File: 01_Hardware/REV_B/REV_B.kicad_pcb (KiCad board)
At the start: 2 copper layers, 65 x 30 mm, 79 parts, among them J1 RaspberryPi, J10 Conn_01x03, J11 Conn_01x03, J12 Conn_01x03, J13 Conn_01x08, J2 Conn_01x02, J3 Conn_01x02, J4 Conn_01x02, J5 Conn_01x08, J6 Conn_02x04_Counter_Clockwise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

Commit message: Routing in progress
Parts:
- C1: moved to B.Cu
- moved R18 17.4 mm to (40.1, 17.7)
- moved R19 15.5 mm to (40.1, 19.3)
- moved R20 14.3 mm to (40.1, 20.8)
- moved R29 11.4 mm to (34.5, 17.4), turned to 0 degrees
- moved C3 10.5 mm to (51.6, 18.3)
- moved R46 7.09 mm to (34.5, 20.8)
- moved R47 7.09 mm to (34.5, 19.1)
- moved R9 5.98 mm to (32.3, 9.53), turned to 270 degrees
- moved U3 4.24 mm to (37.7, 11.3)
- moved J6 2.95 mm to (34.8, 13.5), turned to 270 degrees
- moved J9 2.16 mm to (31.2, 22.9)
- moved J7 2.03 mm to (37.6, 22.9)
- moved J8 1.91 mm to (34.5, 22.9)
- moved R28 1.48 mm to (44.6, 19.2)
- moved R27 1.27 mm to (44.6, 17.7)
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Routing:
- net +3V3: track 71.9 -> 147.2 mm, vias 4 -> 6
- net +BATT: track 0.00 -> 30.0 mm, vias 0 -> 2
- net +5V: track 58.2 -> 85.0 mm
- net Net-(D1-Pad3): track 0.00 -> 25.3 mm, vias 0 -> 1
- net Net-(D1-Pad2): track 0.00 -> 23.4 mm, vias 0 -> 1
- net Net-(D1-Pad4): track 0.00 -> 21.8 mm, vias 0 -> 1
- net Net-(J1-Pad35): track 0.00 -> 16.0 mm
- net Net-(J3-Pad2): track 0.00 -> 15.7 mm
- net GND: track 0.00 -> 15.6 mm, vias 0 -> 6
- net Net-(J1-Pad40): track 0.00 -> 15.0 mm, vias 0 -> 1
- net Net-(C10-Pad1): track 3.94 -> 17.8 mm
- net Net-(J1-Pad37): track 0.00 -> 13.6 mm, vias 0 -> 1
- net Net-(J1-Pad36): track 0.00 -> 13.5 mm
- net Net-(J5-Pad8): track 0.00 -> 12.6 mm, vias 0 -> 1
- net Net-(J1-Pad32): track 0.00 -> 12.4 mm
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
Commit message: Routing almost done
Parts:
- moved C4 0.76 mm to (25.9, 8.26)
- moved R10 0.76 mm to (24.1, 8.26)
- moved R1 0.38 mm to (27.9, 8.26)
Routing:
- net SPI0_CS1_LV: track 0.00 -> 61.9 mm, vias 0 -> 3
- net GND: track 15.6 -> 75.2 mm, vias 6 -> 13
- net I2C1_SDA_HV: track 7.45 -> 56.6 mm
- net SPI0_MISO_LV: track 1.81 -> 50.2 mm, vias 0 -> 4
- net +5V: track 85.0 -> 129.1 mm, vias 4 -> 7
- net SPI0_CLK_LV: track 0.00 -> 40.3 mm, vias 0 -> 1
- net SPI0_MOSI_LV: track 1.88 -> 37.6 mm, vias 0 -> 2
- net I2C1_SCL_HV: track 12.2 -> 40.7 mm, vias 0 -> 2
- net Net-(J6-Pad8): track 0.00 -> 20.5 mm, vias 0 -> 1
- net Net-(J1-Pad24): track 0.00 -> 20.5 mm
- net Net-(J6-Pad2): track 0.00 -> 18.6 mm, vias 0 -> 1
- net Net-(J6-Pad4): track 0.00 -> 18.5 mm, vias 0 -> 1
- net Net-(J6-Pad6): track 0.00 -> 18.2 mm, vias 0 -> 1
- net Net-(R46-Pad2): track 9.14 -> 26.9 mm, vias 2 -> 0
- net Net-(J6-Pad7): track 0.00 -> 17.5 mm, vias 0 -> 1
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
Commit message: routing done
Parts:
- moved C3 0.85 mm to (51.9, 17.5)
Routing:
- net GND: track 75.2 -> 82.0 mm, vias 13 -> 17
- net Net-(J1-Pad37): track 13.7 -> 16.5 mm
- net +3V3: track 156.4 -> 159.0 mm
- net Net-(J1-Pad38): track 9.13 -> 11.3 mm
- net Net-(J6-Pad8): track 20.5 -> 18.6 mm
- net SPI0_MISO_LV: track 50.2 -> 48.4 mm

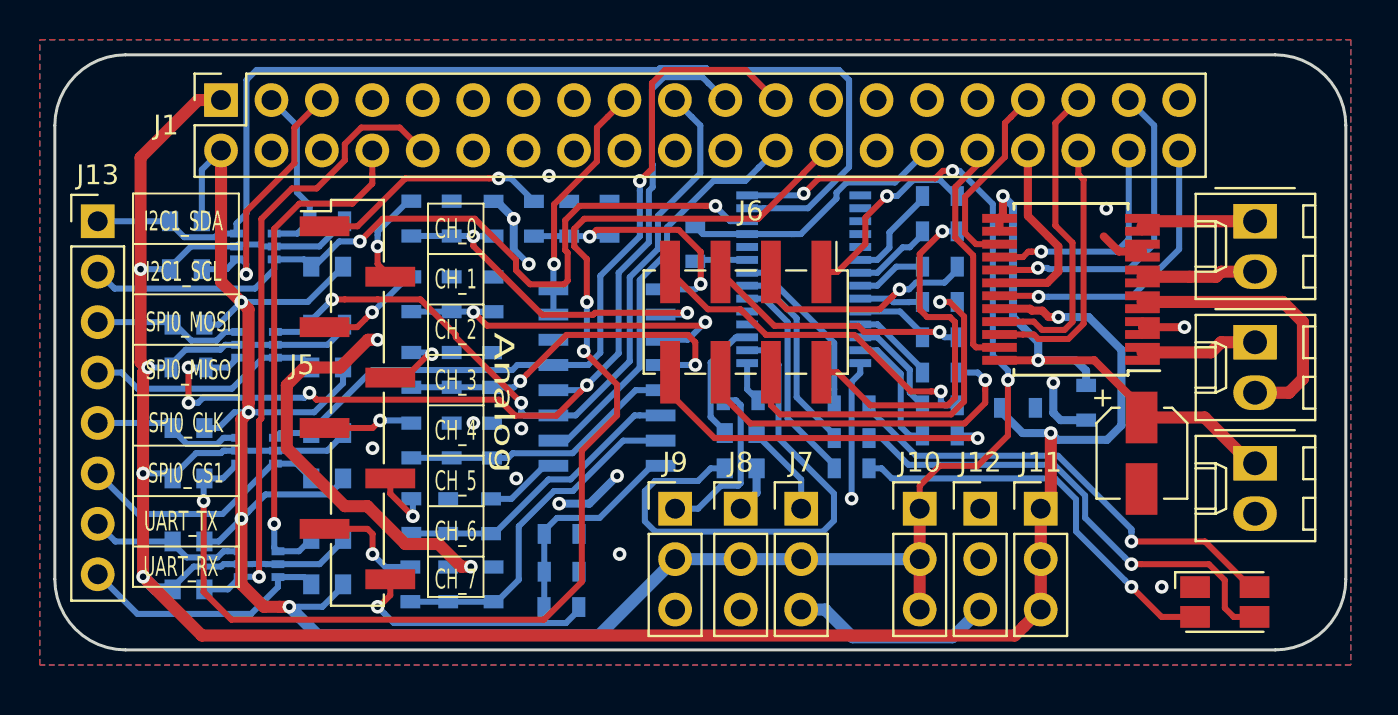
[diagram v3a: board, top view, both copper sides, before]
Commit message: Taster added. routing not done
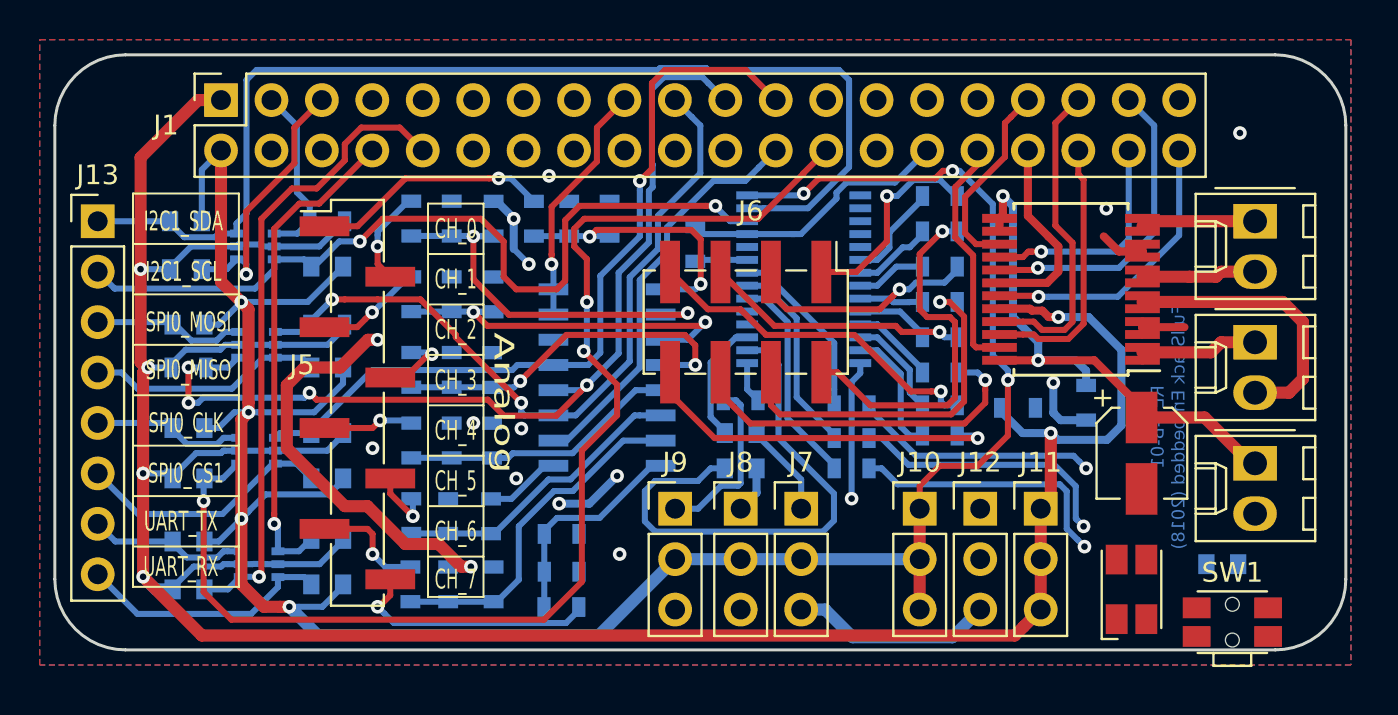
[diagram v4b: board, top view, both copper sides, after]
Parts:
- added R48: 1k, Resistor_SMD:R_0603_1608Metric, B.Cu at (58.8, 25.7)
- added SW1: SW_Push, Button_Switch_SMD:SW_SPST_EVQP7C, F.Cu at (59.3, 28.6)
- moved D1 4.74 mm to (54.2, 26.9), turned to 90 degrees
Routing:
- net Net-(D1-Pad2): track 23.7 -> 12.3 mm
- net Net-(D1-Pad3): track 24.6 -> 13.6 mm
- net Net-(D1-Pad4): track 20.6 -> 13.6 mm
- net Net-(C5-Pad1): track 19.3 -> 20.3 mm
- net UART_TX_LV: track 25.8 -> 24.8 mm
- net I2C1_SCL_HV: track 40.7 -> 41.5 mm
- net Net-(J6-Pad1): track 9.87 -> 10.4 mm
- net Net-(J1-Pad37): track 16.5 -> 15.9 mm
- net GND: vias 17 -> 16
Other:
- board text added: "REV-B-01 FullStack Embedded (2018)"

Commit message: routing in progress
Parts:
- moved R41 0.86 mm to (6.48, 23.7)
- moved J2 0.84 mm to (61.3, 20.4)
- moved J3 0.84 mm to (61.3, 14.4)
- moved J4 0.84 mm to (61.3, 8.26)
- moved R48 0.84 mm to (59.6, 25.5)
- moved U7 0.77 mm to (9.97, 25.0)
- moved R36 0.74 mm to (13.5, 23.7)
- moved R37 0.68 mm to (6.48, 26.3)
- moved D1 0.60 mm to (53.9, 27.4)
- moved R34 0.46 mm to (13.5, 18.7)
- moved R43 0.46 mm to (13.5, 11.0)
- moved R45 0.46 mm to (13.5, 26.3)
- moved R31 0.41 mm to (6.48, 16.1)
- moved R42 0.41 mm to (13.5, 16.1)
- moved R35 0.32 mm to (6.48, 21.1)
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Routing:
- net +3V3: track 159.1 -> 72.6 mm, vias 7 -> 5
- net GND: track 82.0 -> 0.00 mm, vias 16 -> 0
- net SPI0_CS1_LV: track 62.0 -> 2.00 mm, vias 3 -> 0
- net +5V: track 129.1 -> 78.9 mm, vias 7 -> 5
- net I2C1_SDA_HV: track 56.6 -> 7.34 mm
- net SPI0_MISO_LV: track 48.4 -> 1.98 mm, vias 4 -> 0
- net SPI0_CLK_LV: track 40.0 -> 1.97 mm, vias 1 -> 0
- net SPI0_MOSI_LV: track 37.7 -> 1.85 mm, vias 2 -> 0
- net +BATT: track 29.5 -> 0.00 mm, vias 2 -> 0
- net I2C1_SCL_HV: track 41.5 -> 12.2 mm, vias 2 -> 0
- net Net-(R46-Pad2): track 26.9 -> 0.00 mm
- net Net-(J1-Pad24): track 20.6 -> 0.00 mm
- net Net-(J6-Pad2): track 18.6 -> 0.00 mm, vias 1 -> 0
- net Net-(J6-Pad8): track 18.6 -> 0.00 mm, vias 1 -> 0
- net Net-(J6-Pad4): track 18.5 -> 0.00 mm, vias 1 -> 0
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
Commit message: Routing done
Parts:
- added C12: 0.33u, Capacitor_SMD:C_0603_1608Metric, F.Cu at (21.9, 28.0)
- added C13: 10n, Capacitor_SMD:C_0603_1608Metric, F.Cu at (31.1, 28.0)
- added U8: L7805, Package_TO_SOT_SMD:TO-252-3_TabPin2, F.Cu at (27.0, 23.9)
- moved J9 7.89 mm to (39.1, 23.3)
- moved R8 3.17 mm to (28.3, 25.6), turned to 270 degrees
- moved R48 2.89 mm to (56.8, 25.1), turned to 270 degrees
- moved R17 2.36 mm to (24.6, 25.6), turned to 90 degrees
- moved R47 1.97 mm to (35.2, 20.9)
- moved R46 1.91 mm to (35.2, 19.1)
- moved J7 1.35 mm to (36.3, 23.3)
- moved J8 1.11 mm to (33.5, 23.3)
- moved D1 1.00 mm to (53.3, 26.6)
- moved C1 0.99 mm to (49.5, 17.5), turned to 270 degrees
- moved C11 0.97 mm to (26.4, 25.6), turned to 270 degrees
- moved R21 0.95 mm to (43.6, 7.18)
- moved R29 0.64 mm to (35.2, 17.3), turned to 180 degrees
- moved J10 0.51 mm to (43.8, 23.3)
- moved J11 0.51 mm to (49.4, 23.3)
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- renumbered SW1 to PB
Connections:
- J1 pad 22: (no net) -> PUSH_BUTTON
- PB pad 1: +3V3 -> Net-(R48-Pad2)
- PB pad 2: Net-(R48-Pad2) -> +3V3
- R48 pad 1: (no net) -> PUSH_BUTTON
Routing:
- net +3V3: track 72.6 -> 149.2 mm, vias 5 -> 9
- net SPI0_MISO_LV: track 1.98 -> 70.7 mm, vias 0 -> 3
- net +BATT: track 0.00 -> 66.4 mm, vias 0 -> 1
- net SPI0_CS1_LV: track 2.00 -> 67.8 mm, vias 0 -> 2
- net +5V: track 78.9 -> 127.5 mm, vias 5 -> 7
- net PUSH_BUTTON: track 0.00 -> 38.7 mm
- net SPI0_CLK_LV: track 1.97 -> 39.8 mm, vias 0 -> 3
- net SPI0_MOSI_LV: track 1.85 -> 37.7 mm, vias 0 -> 1
- net I2C1_SDA_HV: track 7.34 -> 35.7 mm, vias 0 -> 2
- net Net-(J6-Pad7): track 0.00 -> 27.1 mm, vias 0 -> 1
- net I2C1_SCL_HV: track 12.2 -> 37.6 mm
- net Net-(J6-Pad8): track 0.00 -> 23.5 mm, vias 0 -> 1
- net Net-(J6-Pad5): track 0.00 -> 22.1 mm, vias 0 -> 1
- net Net-(J1-Pad24): track 0.00 -> 21.7 mm, vias 0 -> 1
- net Net-(J6-Pad3): track 0.00 -> 20.7 mm, vias 0 -> 1
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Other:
- board text added: "+3.3V"
- board text added: "+5V"
- board text added: "0"
- board text added: "1"
- board text added: "2"
- board text added: "3"
- board text added: "4"
- board text added: "5"
- board text added: "6"
- board text added: "7"
- board text added: "BATTERY"
- board text added: "GND"
- board text added: "J10"
- board text added: "J11"
- board text added: "J12"
- board text added: "J7"
- board text added: "J8"
- board text added: "J9"
- board text added: "MOTOR1"
- board text added: "MOTOR2"
- board text added: "PWM10"
- board text added: "PWM8"
- board text added: "PWM9"
- board text added: "PWMs:"

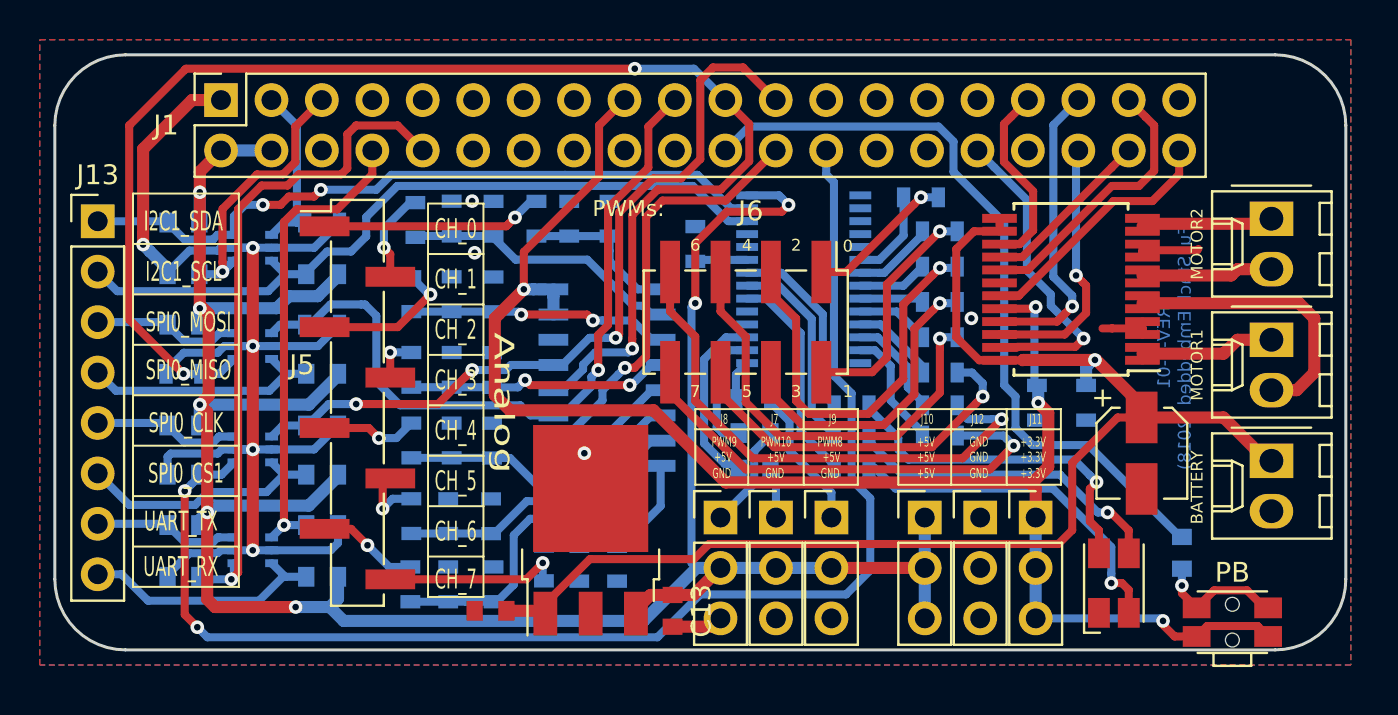
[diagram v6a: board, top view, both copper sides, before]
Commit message: Routing done. Ready to be manufactured
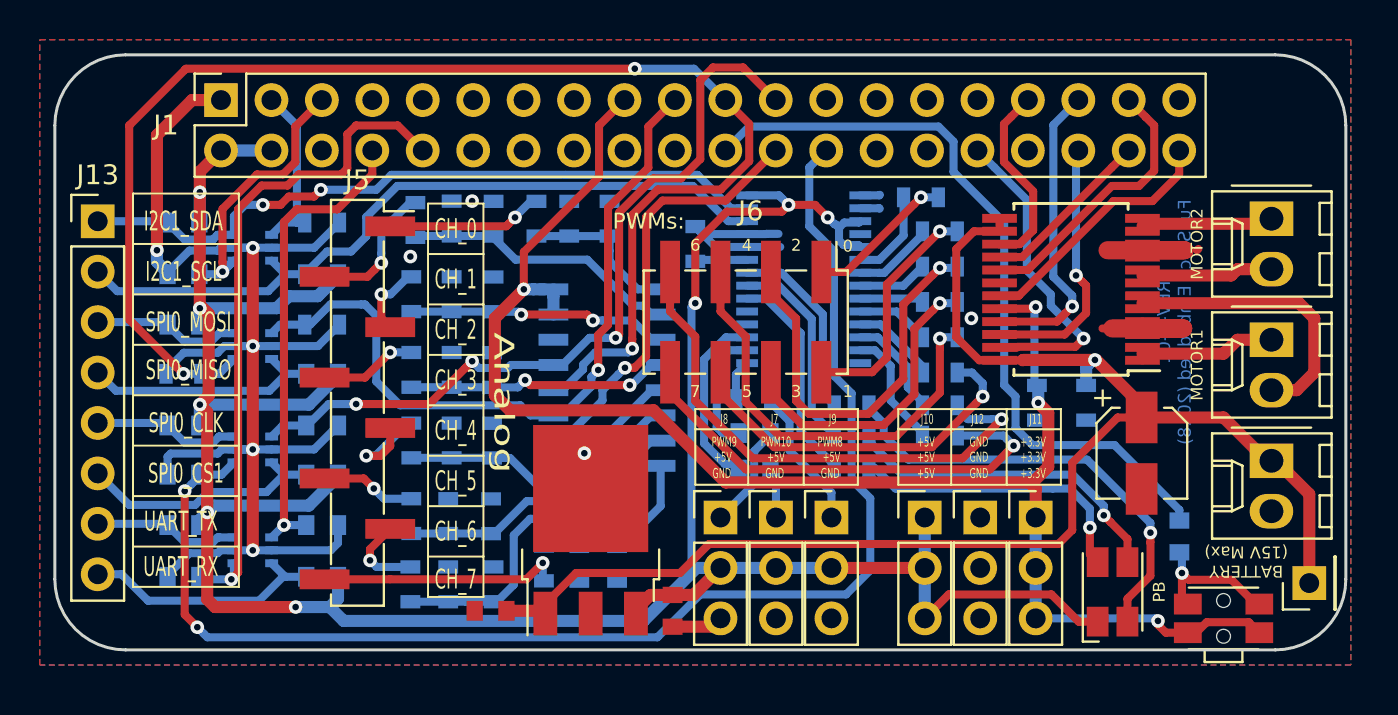
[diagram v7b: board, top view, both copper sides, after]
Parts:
- removed PB: SW_Push, Button_Switch_SMD:SW_SPST_EVQP7C
- added J14: Conn_01x01, Connector_PinHeader_2.54mm:PinHeader_1x01_P2.54mm_Vertical, F.Cu at (63.2, 26.6)
- added PB1: SW_Push, Button_Switch_SMD:SW_SPST_EVQP7C, F.Cu at (58.9, 28.4)
- D1: value LED_CRGB -> LED_ARGB
- J5: footprint Connector_PinHeader_2.54mm:PinHeader_1x08_P2.54mm_Vertical_SMD_Pin1Left -> Connector_PinHeader_2.54mm:PinHeader_1x08_P2.54mm_Vertical_SMD_Pin1Right
- moved R48 0.84 mm to (56.6, 24.3)
- moved D1 0.45 mm to (53.3, 27.1)
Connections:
- D1 pad 1: GND -> +5V
- R18 pad 1: Net-(D1-Pad2) -> Net-(D1-Pad4)
- R20 pad 1: Net-(D1-Pad4) -> Net-(D1-Pad2)
- U3 pad 1: (no net) -> GND
- U3 pad 2: (no net) -> GND
- U3 pad 24: (no net) -> GND
- U3 pad 3: (no net) -> +5V
- U3 pad 4: (no net) -> GND
- U3 pad 5: (no net) -> +5V
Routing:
- net GND: track 10.7 -> 29.1 mm
- net +5V: track 127.5 -> 143.4 mm, vias 7 -> 8
- net +BATT: track 66.4 -> 73.5 mm
- net Net-(D1-Pad4): track 17.8 -> 22.5 mm
- net Net-(J5-Pad3): track 7.35 -> 3.71 mm
- net Net-(J5-Pad8): track 8.95 -> 12.3 mm
- net Net-(J5-Pad1): track 11.1 -> 7.77 mm
- net Net-(D1-Pad2): track 17.4 -> 14.8 mm
- net Net-(J5-Pad4): track 2.34 -> 4.91 mm
- net Net-(J5-Pad2): track 4.51 -> 6.88 mm
- net Net-(J5-Pad6): track 3.34 -> 4.79 mm
- net Net-(R48-Pad2): track 6.05 -> 7.33 mm
- net Net-(J5-Pad7): track 5.12 -> 4.18 mm
- net SPI0_CS1_LV: track 67.8 -> 68.5 mm
- net +3V3: track 149.2 -> 148.6 mm
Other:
- board text added: "BATTERY (15V Max)"
- board text added: "PB"
- board text removed: "BATTERY"

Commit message: Last Modification: Jumper J5 long pad smd used
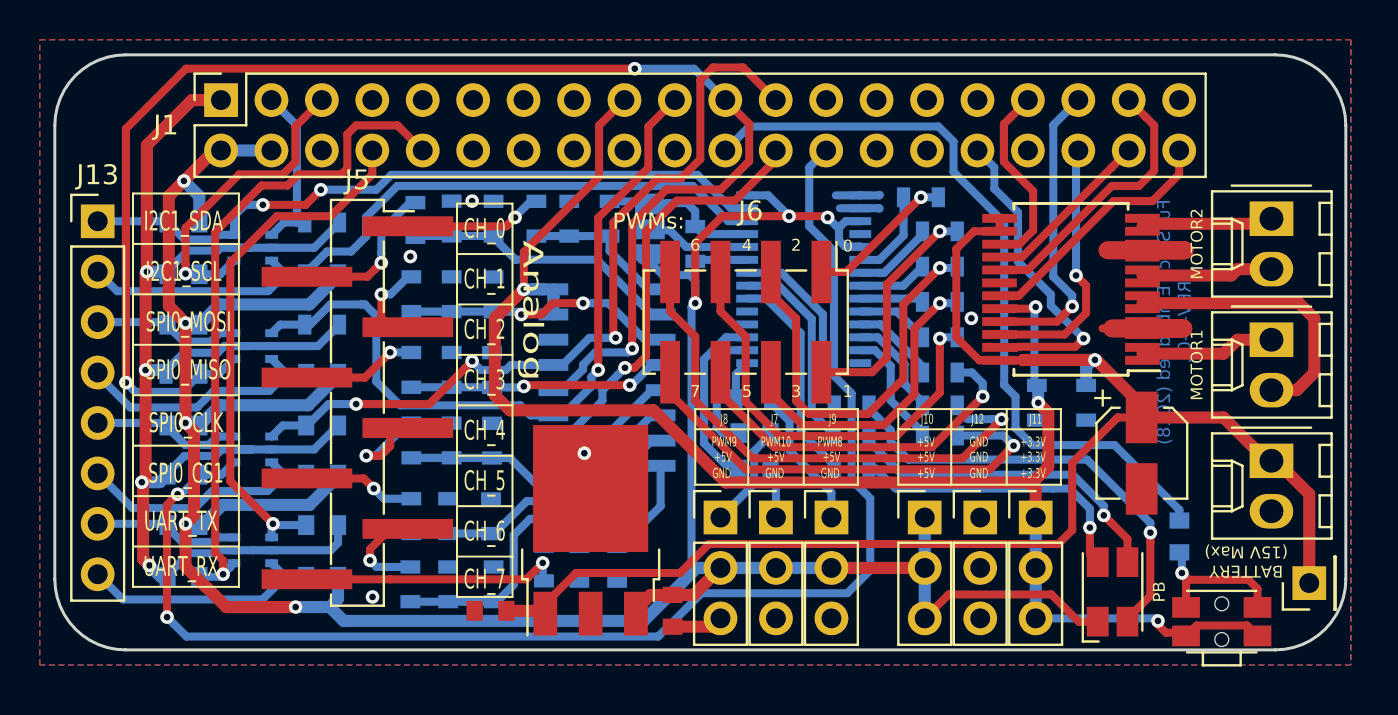
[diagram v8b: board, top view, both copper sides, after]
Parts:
- removed PB1: SW_Push, Button_Switch_SMD:SW_SPST_EVQP7C
- added JP1: Jumper_3_Open, Jumper:SolderJumper-3_P1.3mm_Open_RoundedPad1.0x1.5mm, B.Cu at (30.0, 8.79)
- added SW1: SW_Push, Button_Switch_SMD:SW_SPST_EVQP7C, F.Cu at (58.8, 28.5)
- J5: footprint Connector_PinHeader_2.54mm:PinHeader_1x08_P2.54mm_Vertical_SMD_Pin1Right -> FSE:PinHeader_1x08_P2.54mm_LongPad_Vertical_SMD_Pin1Right
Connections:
- U3 pad 24: GND -> Net-(JP1-Pad2)
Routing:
- net +5V: track 143.4 -> 150.5 mm
- net Net-(JP1-Pad2): track 0.00 -> 5.27 mm
- net +3V3: track 148.6 -> 152.3 mm, vias 9 -> 8
- net UART_TX_LV: track 23.9 -> 26.7 mm
- net SPI0_MISO_LV: track 70.7 -> 73.2 mm
- net GND: track 29.1 -> 30.6 mm, vias 4 -> 5
- net SPI0_CS1_LV: track 68.5 -> 69.9 mm
- net I2C1_SCL_LV: track 14.3 -> 15.6 mm
- net Net-(R48-Pad2): track 7.33 -> 8.13 mm
- net Net-(J13-Pad4): track 12.3 -> 13.1 mm
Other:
- board text added: "FullStack Embedded (2018) REV-B-01"
- board text removed: "REV-B-01 FullStack Embedded (2018)"
